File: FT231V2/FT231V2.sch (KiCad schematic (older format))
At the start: 20 parts, among them J1 Conn_01x06, P1 USB_C_Plug_USB2.0, U1 FT231XQ

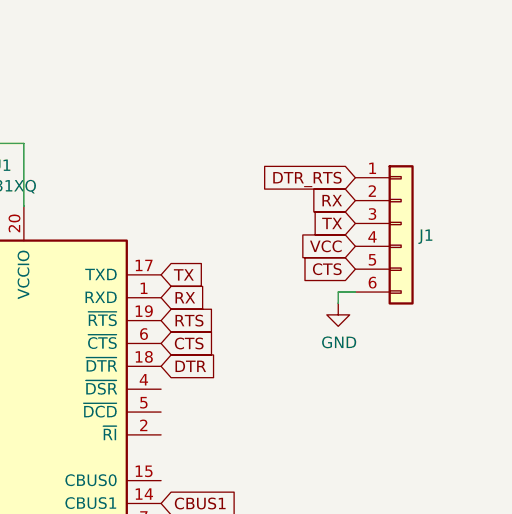
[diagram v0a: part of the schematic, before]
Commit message: SiRUSB Updates
USB-C 3D Renders Added and Pictures Updated
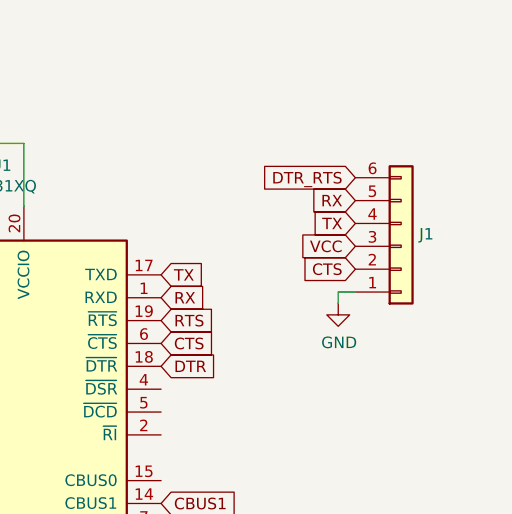
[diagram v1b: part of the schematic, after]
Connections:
- net CTS: now also J1.2 (Pin_2); no longer J1.5 (Pin_5)
- net DTR_RTS: now also J1.6 (Pin_6); no longer J1.1 (Pin_1)
- net GND: now also J1.1 (Pin_1); no longer J1.6 (Pin_6)
- net RX: now also J1.5 (Pin_5); no longer J1.2 (Pin_2)
- net TX: now also J1.4 (Pin_4); no longer J1.3 (Pin_3)
- net VCC: now also J1.3 (Pin_3); no longer J1.4 (Pin_4)
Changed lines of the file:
@@
 L Connector_Generic:Conn_01x06 J1
 U 1 1 5E4934CD
-P 7325 1550
-F 0 "J1" H 7404 1497 50  0000 L CNN
-F 1 "Conn_01x06" H 7404 1452 50  0001 L CNN
-F 2 "Connector_PinHeader_2.54mm:PinHeader_1x06_P2.54mm_Vertical" H 7325 1550 50  0001 C CNN
-F 3 "~" H 7325 1550 50  0001 C CNN
-	1    7325 1550
-	1    0    0    -1
+P 7325 1650
+F 0 "J1" H 7404 1597 50  0000 L CNN
+F 1 "Conn_01x06" H 7404 1552 50  0001 L CNN
+F 2 "Connector_PinHeader_2.54mm:PinHeader_1x06_P2.54mm_Vertical" H 7325 1650 50  0001 C CNN
+F 3 "~" H 7325 1650 50  0001 C CNN
+	1    7325 1650
+	1    0    0    1
 $EndComp
 Text GLabel 7125 1550 0    50   Input ~ 0

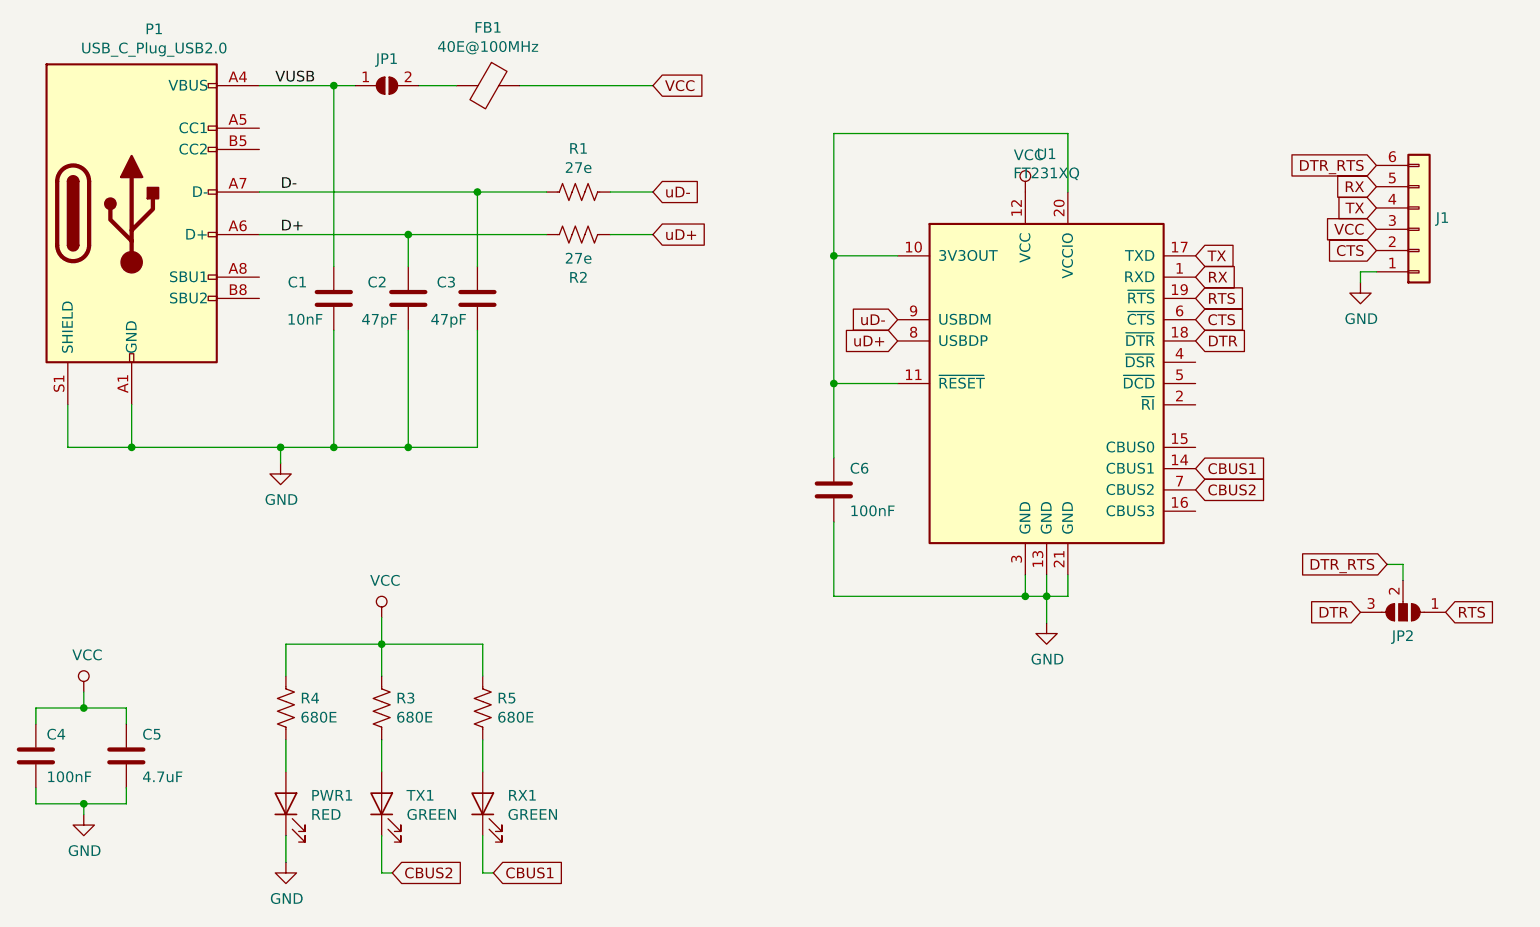
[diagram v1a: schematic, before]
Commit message: SirUSB Board Revisions
Removed MicroUSB Versions of FT230 and FT231, SolderPaste Layer Adjusted to -0.05mm, Silkscreens optimised, OSHW logo added.
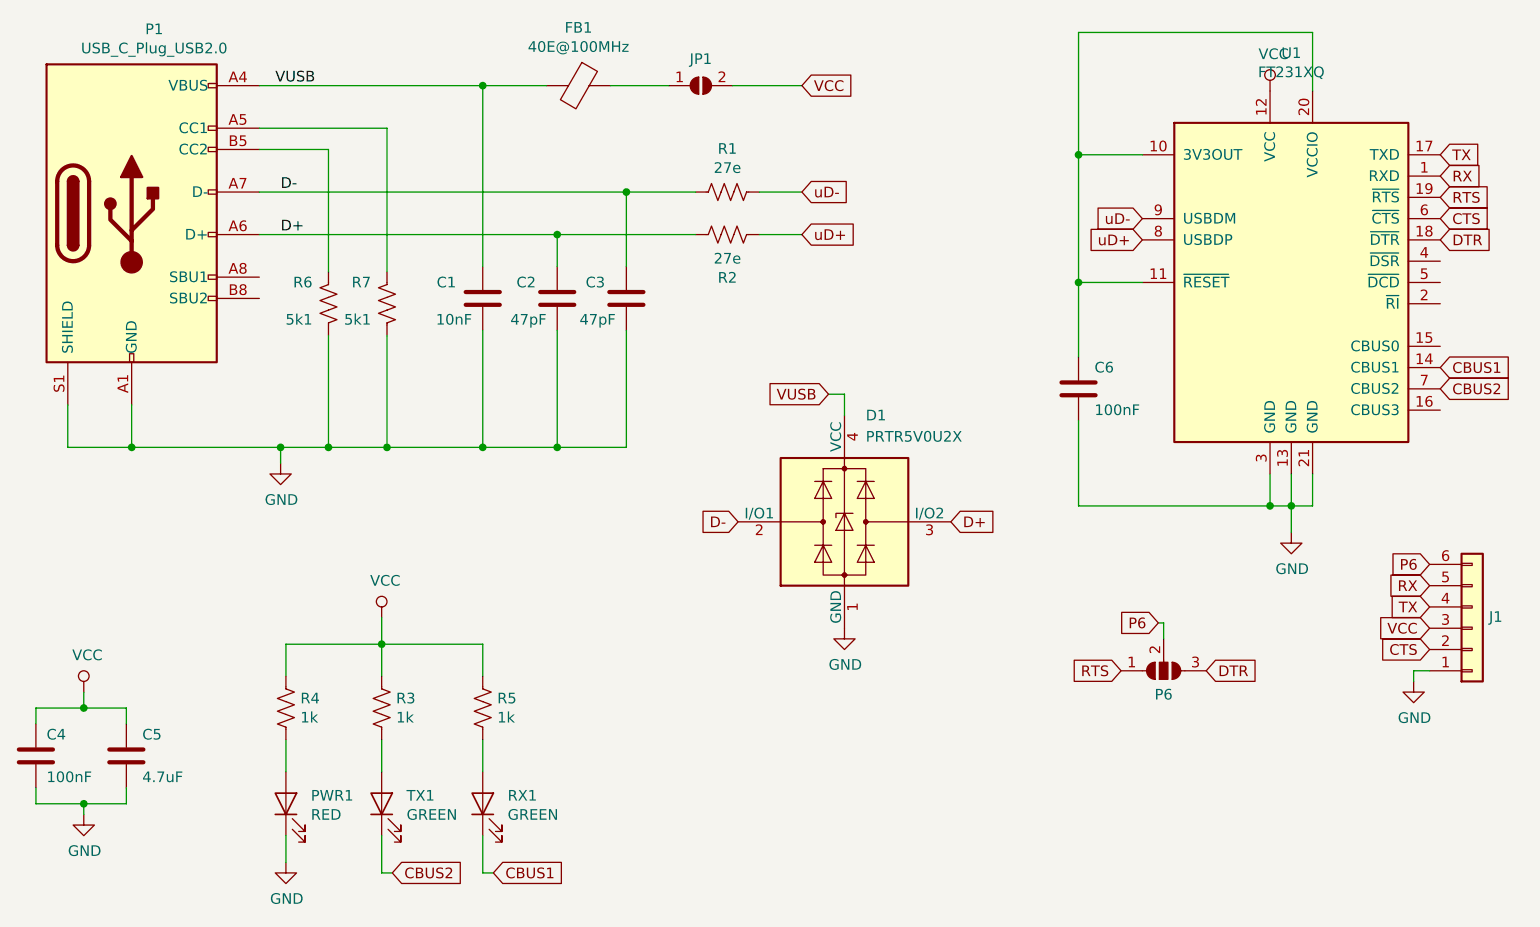
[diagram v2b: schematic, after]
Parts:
- removed JP2: SolderJumper_3_Open, Jumper:SolderJumper-3_P1.3mm_Open_RoundedPad1.0x1.5mm, symbol Jumper:SolderJumper_3_Open
- added D1: PRTR5V0U2X, SirBoardLibrary:SOT-143, symbol Power_Protection:PRTR5V0U2X
- added P6: SolderJumper_3_Open, Jumper:SolderJumper-3_P1.3mm_Open_RoundedPad1.0x1.5mm, symbol Jumper:SolderJumper_3_Open
- added R6, R7: 5k1, Resistor_SMD:R_0603_1608Metric, symbol Device:R_US
- R3, R4, R5: value 680E -> 1k; Part C269441 -> C25585
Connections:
- net D+: now also D1.3 (I/O2)
- net D-: now also D1.2 (I/O1)
- net DTR: now also P6.3 (B)
- net GND: now also D1.1 (GND), R6.2, R7.2
- net RTS: now also P6.1 (A)
- net VCC: now also JP1.2 (B); no longer FB1.1
- net VUSB: now also FB1.2, D1.4 (VCC); no longer JP1.1 (A)
- net at P1.A5 (CC1): now also R7.1
- net at P1.B5 (CC2): now also R6.1
- net DTR_RTS renamed P6
- net P6: now also P6.2 (C)
- new net: FB1.1, JP1.1 (A)
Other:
- moved on the sheet: C1, C2, C3, C6, FB1, J1, JP1, R1, R2
